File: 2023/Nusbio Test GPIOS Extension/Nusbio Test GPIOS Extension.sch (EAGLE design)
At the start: 7 parts

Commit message: Nusbio /2 v3
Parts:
- removed SOIC8_208MIL_EEPROM: (no value), microbuilder:SPIFLASH_SOIC8208MIL
- added SPI_SOIC_8_FLASH: 25AA080SN, microchip:25AA080SN
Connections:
- net CS: now also SPI_SOIC_8_FLASH.!CS; no longer SOIC8_208MIL_EEPROM.SSEL
- net GND: now also SPI_SOIC_8_FLASH.GND; no longer SOIC8_208MIL_EEPROM.VSS
- net MISO: now also SPI_SOIC_8_FLASH.SO; no longer SOIC8_208MIL_EEPROM.MISO
- net MOSI: now also SPI_SOIC_8_FLASH.SI; no longer SOIC8_208MIL_EEPROM.MOSI
- net SCK: now also SPI_SOIC_8_FLASH.SCK; no longer SOIC8_208MIL_EEPROM.SCK
- net VCC: now also SPI_SOIC_8_FLASH.!HOLD, SPI_SOIC_8_FLASH.!WP, SPI_SOIC_8_FLASH.VCC; no longer SOIC8_208MIL_EEPROM.#HOLD/IO3, SOIC8_208MIL_EEPROM.#WP/IO2, SOIC8_208MIL_EEPROM.VCC
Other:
- moved on the sheet: GPIO_IN, GPIO_OUT

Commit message: Test Esxtension
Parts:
- removed GPIO_OUT: PINHD-1X10, adafruit:PINHD-1X10
- removed SPI_SOIC_8_FLASH: 25AA080SN, microchip:25AA080SN
- added GPIO_0_4_CONN, GPIO_1_5_CONN: (no value), microbuilder:SOLDERJUMPERREFLOW
- added LED_0, LED_1, LED_2, LED_3: (no value), adafruit:LEDSMT1206
- added R_2K1, R_2K2, R_2K3, R_2K4: (no value), adafruit:R-US_R1206
- renumbered USE_CS_3 to GPIO_3_7_CONN, USE_CS_4 to GPIO_2_6_CONN
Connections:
- removed net CS: GPIO_2_6_CONN.2, GPIO_3_7_CONN.2, SPI_SOIC_8_FLASH.!CS
- removed net CS_3: GPIO_3_7_CONN.1, GPIO_IN.4, GPIO_OUT.4
- removed net CS_4: GPIO_2_6_CONN.1, GPIO_IN.5, GPIO_OUT.5
- removed net GPIO8: GPIO_IN.8, GPIO_OUT.8
- removed net MISO: GPIO_IN.3, GPIO_OUT.3, SPI_SOIC_8_FLASH.SO
- removed net MOSI: GPIO_IN.2, GPIO_OUT.2, SPI_SOIC_8_FLASH.SI
- removed net SCK: GPIO_IN.1, GPIO_OUT.1, SPI_SOIC_8_FLASH.SCK
- new net GPIO0: GPIO_0_4_CONN.1, GPIO_IN.1, LED_0.A
- new net GPIO1: GPIO_1_5_CONN.1, GPIO_IN.2, LED_1.A
- new net GPIO2: GPIO_2_6_CONN.1, GPIO_IN.3, LED_2.A
- new net GPIO3: GPIO_3_7_CONN.1, GPIO_IN.4, LED_3.A
- new net GPIO4: GPIO_0_4_CONN.2, GPIO_IN.5
- new net GPIO5: GPIO_1_5_CONN.2, GPIO_IN.6
- new net N$1: LED_0.C, R_2K1.2
- new net N$3: LED_1.C, R_2K2.2
- new net N$4: LED_2.C, R_2K3.2
- new net N$5: LED_3.C, R_2K4.2
- net GND: now also R_2K1.1, R_2K2.1, R_2K3.1, R_2K4.1; no longer GPIO_OUT.10, SPI_SOIC_8_FLASH.GND
- net GPIO6: now also GPIO_2_6_CONN.2, GPIO_IN.7; no longer GPIO_IN.6, GPIO_OUT.6
- net GPIO7: now also GPIO_3_7_CONN.2, GPIO_IN.8; no longer GPIO_IN.7, GPIO_OUT.7
- net VCC: no longer GPIO_OUT.9, SPI_SOIC_8_FLASH.!HOLD, SPI_SOIC_8_FLASH.!WP, SPI_SOIC_8_FLASH.VCC
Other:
- moved on the sheet: GPIO_IN

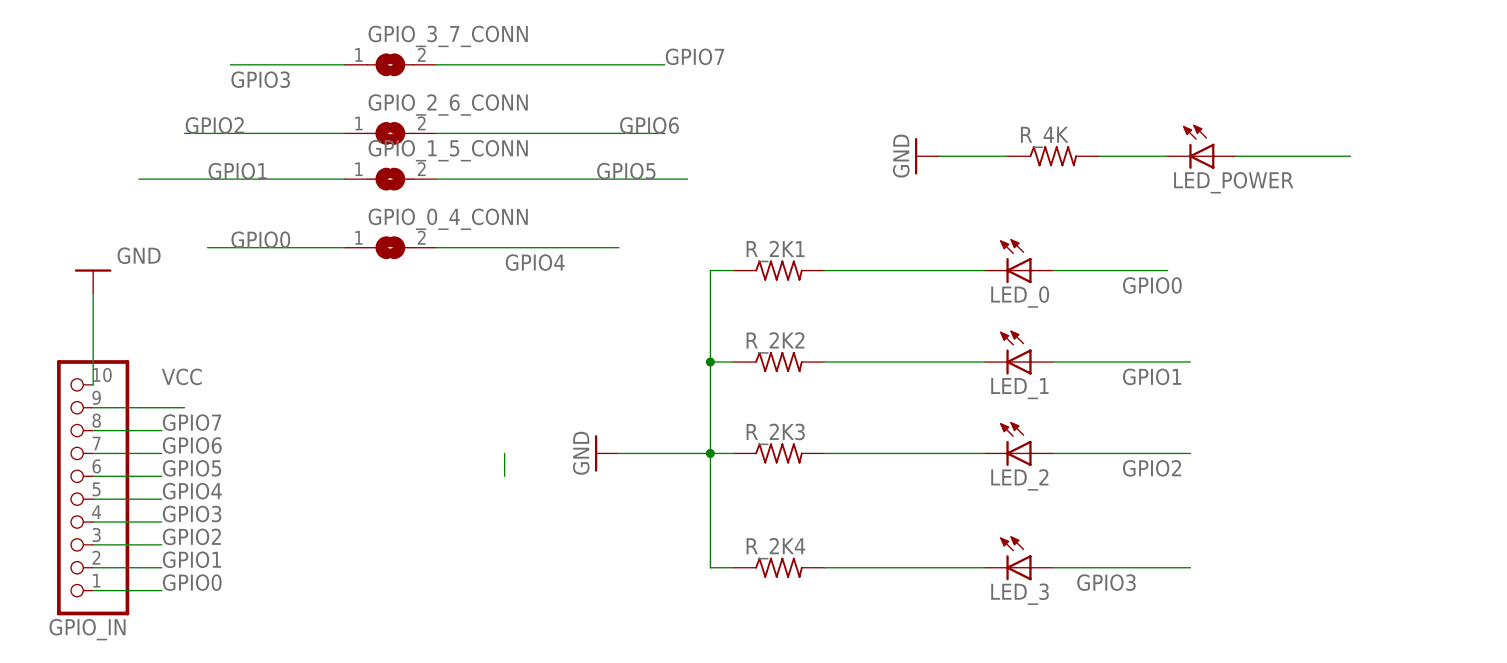
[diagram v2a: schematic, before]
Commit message: Nusbio test extension
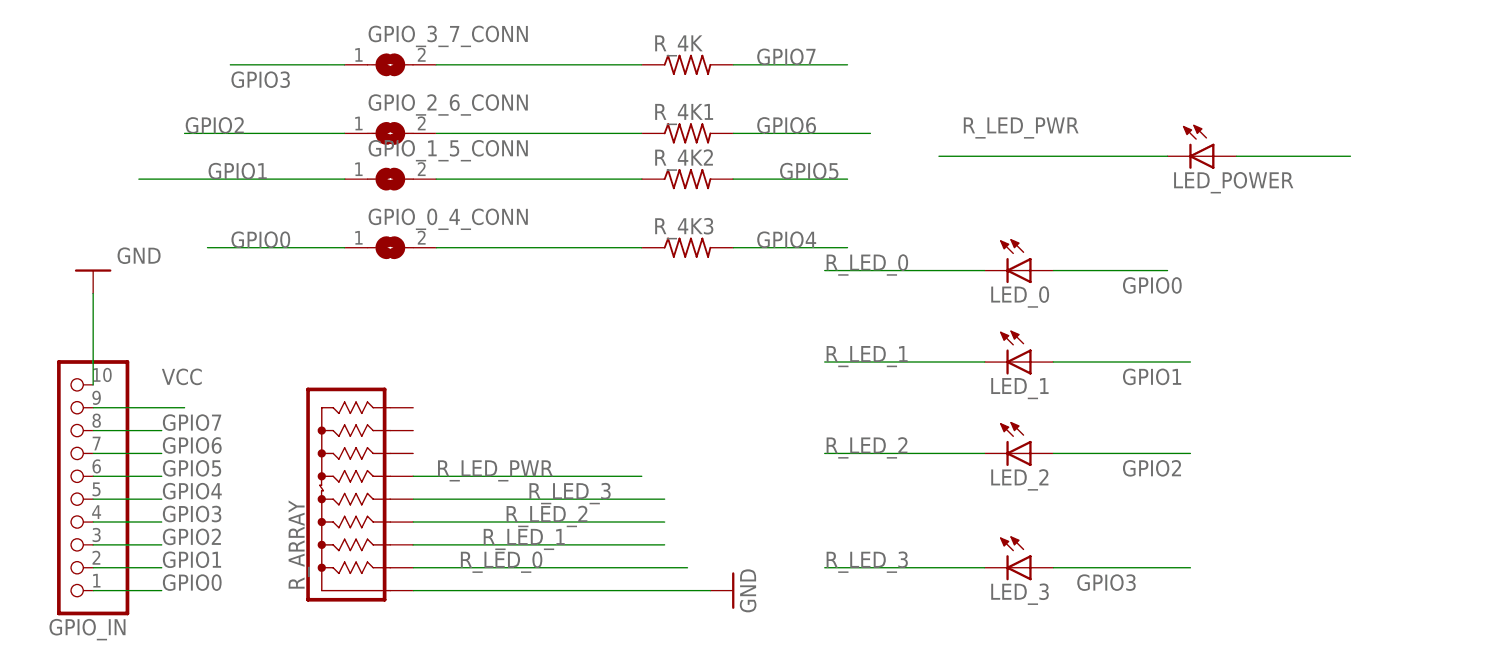
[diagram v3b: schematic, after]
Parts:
- removed R_2K1, R_2K2, R_2K3, R_2K4: (no value), adafruit:R-US_R1206
- added R_4K1, R_4K2, R_4K3: (no value), adafruit:R-US_R1206
- added R_ARRAY: (no value), resistor-sip:4609X
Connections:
- removed net N$5: LED_3.C, R_2K4.2
- new net R_LED_0: LED_0.C, R_ARRAY.2
- new net R_LED_1: LED_1.C, R_ARRAY.3
- new net R_LED_2: LED_2.C, R_ARRAY.4
- new net R_LED_3: LED_3.C, R_ARRAY.5
- new net R_LED_PWR: LED_POWER.C, R_ARRAY.6
- net GND: now also R_ARRAY.1; no longer R_2K1.1, R_2K2.1, R_2K3.1, R_2K4.1, R_4K.1
- net GPIO4: now also R_4K3.2; no longer GPIO_0_4_CONN.2
- net GPIO5: now also R_4K2.2; no longer GPIO_1_5_CONN.2
- net GPIO6: now also R_4K1.2; no longer GPIO_2_6_CONN.2
- net GPIO7: now also R_4K.2; no longer GPIO_3_7_CONN.2
- net N$1: now also GPIO_3_7_CONN.2, R_4K.1; no longer LED_0.C, R_2K1.2
- net N$2: now also GPIO_2_6_CONN.2, R_4K1.1; no longer LED_POWER.C, R_4K.2
- net N$3: now also GPIO_1_5_CONN.2, R_4K2.1; no longer LED_1.C, R_2K2.2
- net N$4: now also GPIO_0_4_CONN.2, R_4K3.1; no longer LED_2.C, R_2K3.2
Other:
- moved on the sheet: R_4K

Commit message: Nusbio test extension
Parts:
- renumbered R_4K to R_4K0
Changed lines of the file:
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@@
 <part name="GPIO_IN" library="adafruit" deviceset="PINHD-1X10" device=""/>
 <part name="GND1" library="supply1" deviceset="GND" device=""/>
-<part name="R_4K" library="adafruit" deviceset="R-US_" device="R1206"/>
+<part name="R_4K0" library="adafruit" deviceset="R-US_" device="R1206"/>
 <part name="LED_POWER" library="adafruit" deviceset="LED" device="SMT1206"/>
 <part name="GPIO_3_7_CONN" library="microbuilder" deviceset="SOLDERJUMPER" device="REFLOW"/>
@@
 <attribute name="VALUE" x="-5.08" y="83.82" size="1.778" layer="96" rot="R180"/>
 </instance>
-<instance part="R_4K" gate="G$1" x="53.34" y="104.14" smashed="yes">
+<instance part="R_4K0" gate="G$1" x="53.34" y="104.14" smashed="yes">
 <attribute name="NAME" x="49.53" y="105.6386" size="1.778" layer="95"/>
 <attribute name="VALUE" x="49.53" y="100.838" size="1.778" layer="96"/>
@@
 </segment>
 <segment>
-<pinref part="R_4K" gate="G$1" pin="2"/>
+<pinref part="R_4K0" gate="G$1" pin="2"/>
 <wire x1="58.42" y1="104.14" x2="71.12" y2="104.14" width="0.1524" layer="91"/>
 <label x="60.96" y="104.14" size="1.778" layer="95"/>
@@
 <segment>
 <pinref part="GPIO_3_7_CONN" gate="1" pin="2"/>
-<pinref part="R_4K" gate="G$1" pin="1"/>
+<pinref part="R_4K0" gate="G$1" pin="1"/>
 <wire x1="25.4" y1="104.14" x2="48.26" y2="104.14" width="0.1524" layer="91"/>
 </segment>
